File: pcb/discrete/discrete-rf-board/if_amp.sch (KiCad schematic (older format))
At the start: 46 parts, among them Q401 NSVT65011MW6T1G, Q402 Q_NPN_BCE, Q403 NSVT65011MW6T1G, U401 NLAS4157DFT2G, U402 NLAS4157DFT2G, U403 NLAS4157DFT2G, U404 NLAS4157DFT2G

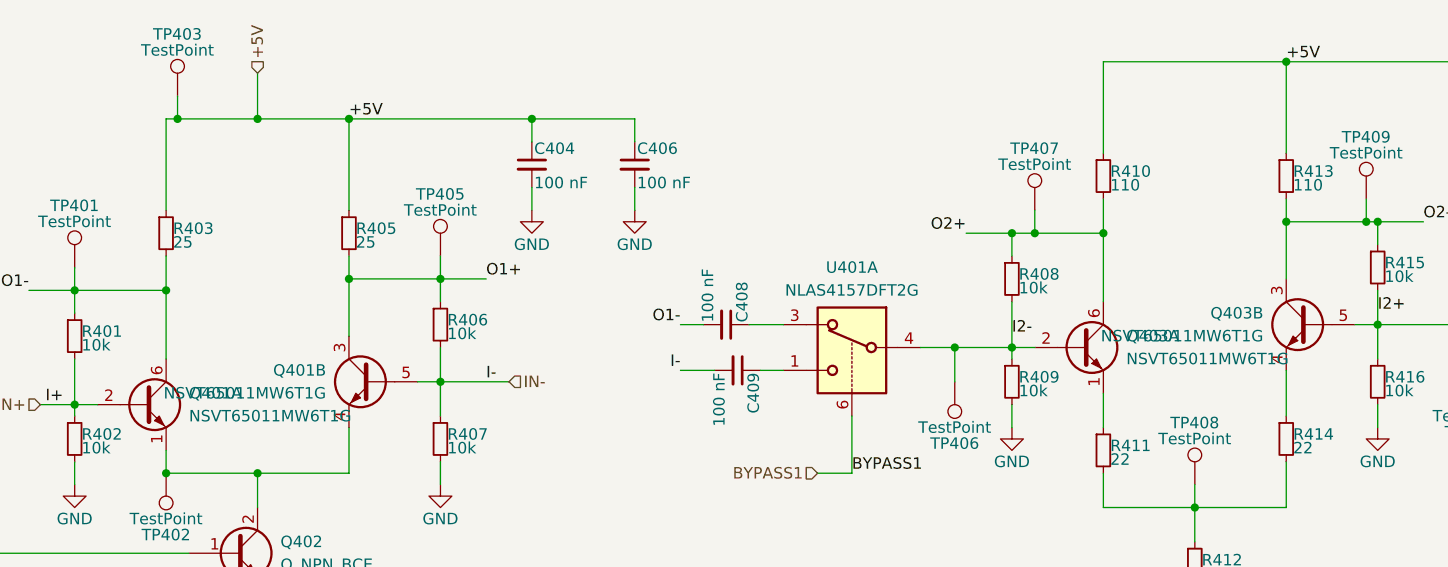
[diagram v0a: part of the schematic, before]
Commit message: Design DAC/ADC stages, pass out all control signals to top sheet
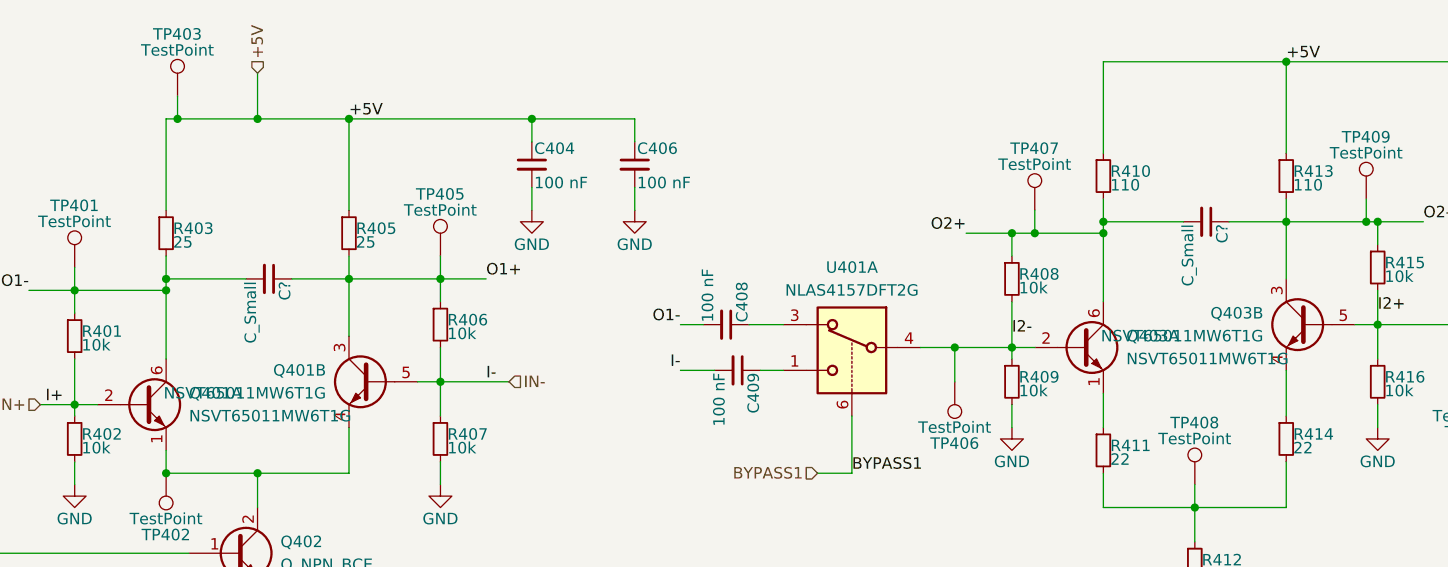
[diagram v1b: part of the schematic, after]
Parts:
- added C? (x2): C_Small, symbol Device:C_Small
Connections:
- net O1+: now also C?.1
- net O1-: now also C?.2
- net O2+: now also C?.2
- net O2-: now also C?.1
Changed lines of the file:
@@
 	1650 2500 2050 2500
 Wire Wire Line
-	2050 2500 2050 2350
+	2050 2500 2050 2450
 Wire Wire Line
 	2050 2800 2050 2500
@@
 	5750 2250 5850 2250
 Wire Wire Line
-	6150 2250 6150 2100
+	6150 2250 6150 2200
 Wire Wire Line
 	6150 2550 6150 2250
@@
 	2850 1750 3650 1750
 Connection ~ 2850 1750
+$Comp
+L Device:C_Small C?
+U 1 1 5DA03B3D
+P 2500 2450
+AR Path="/5CA6B0AA/5CC4DFC2/5DA03B3D" Ref="C?"  Part="1"
+AR Path="/5CA6B0AA/5CC9409A/5DA03B3D" Ref="C?"  Part="1"
+F 0 "C?" H 2510 2520 50  0000 L CNN
+F 1 "C_Small" H 2510 2370 50  0000 L CNN
+F 2 "" H 2500 2450 50  0001 C CNN
+F 3 "~" H 2500 2450 50  0001 C CNN
+	1    2500 2450
+	0    1    1    0
+$EndComp
+Wire Wire Line
+	2600 2450 2850 2450
+Wire Wire Line
+	2400 2450 2050 2450
+Connection ~ 2050 2450
+Wire Wire Line
+	2050 2450 2050 2350
+$Comp
+L Device:C_Small C?
+U 1 1 5DA0FE44
+P 6600 2200
+AR Path="/5CA6B0AA/5CC4DFC2/5DA0FE44" Ref="C?"  Part="1"
+AR Path="/5CA6B0AA/5CC9409A/5DA0FE44" Ref="C?"  Part="1"
+F 0 "C?" H 6610 2270 50  0000 L CNN
+F 1 "C_Small" H 6610 2120 50  0000 L CNN
+F 2 "" H 6600 2200 50  0001 C CNN
+F 3 "~" H 6600 2200 50  0001 C CNN
+	1    6600 2200
+	0    1    1    0
+$EndComp
+Wire Wire Line
+	6700 2200 6950 2200
+Wire Wire Line
+	6500 2200 6150 2200
+Connection ~ 6150 2200
+Wire Wire Line
+	6150 2200 6150 2100
 $EndSCHEMATC

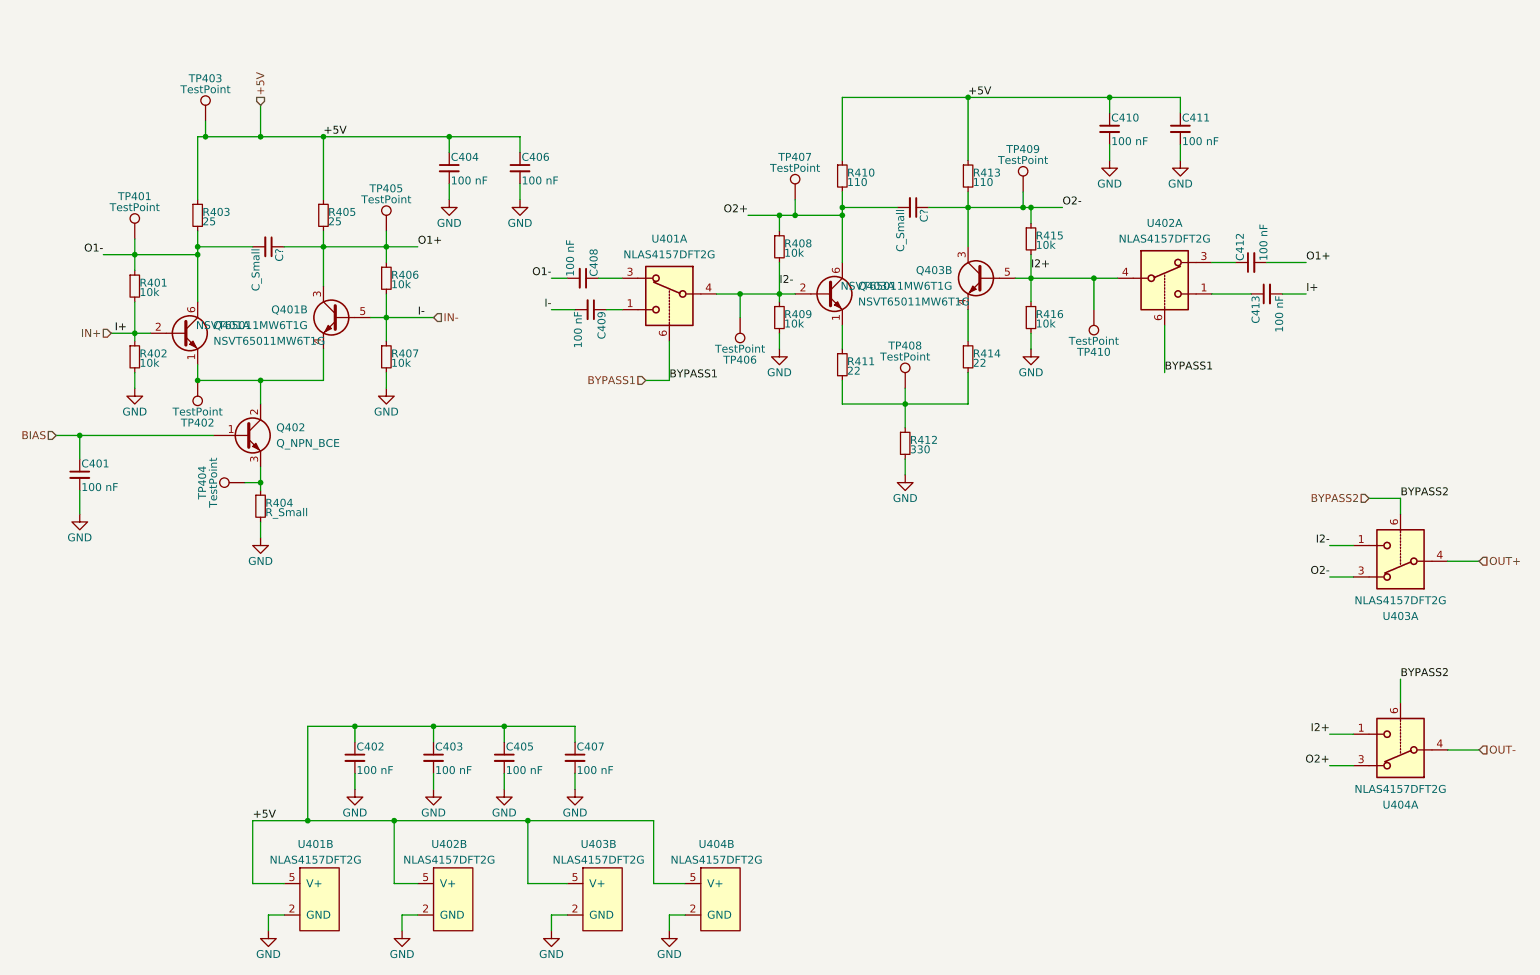
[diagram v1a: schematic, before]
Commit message: Wire out all control signals to connectors TODO PLL charge pump loop, bypass caps in attenuator circuit, antialiasing filter for ADC frontend
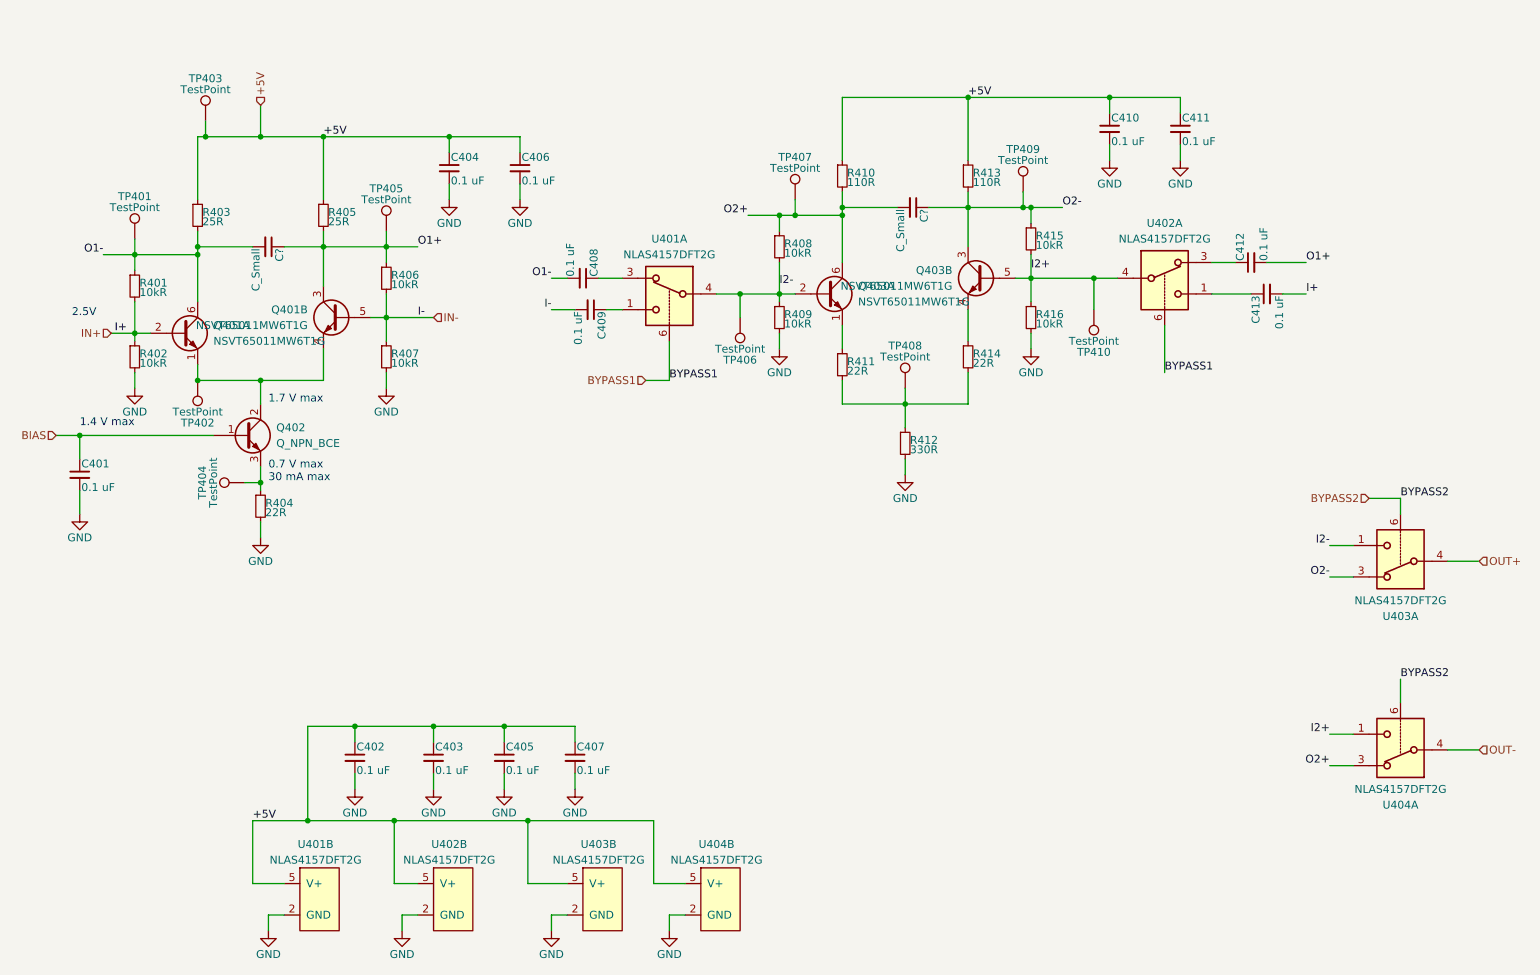
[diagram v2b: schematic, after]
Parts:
- C401, C402, C403, C404, C405, C406, C407, C408, C409, C410, C411, C412, C413: value 100 nF -> 0.1 uF
- R401, R402, R406, R407, R408, R409, R415, R416: value 10k -> 10kR
- R403, R405: value 25 -> 25R
- R404: value R_Small -> 22R
- R410, R413: value 110 -> 110R
- R411, R414: value 22 -> 22R
- R412: value 330 -> 330R
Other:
- note added: "0.7 V max\n30 mA max"
- note added: "1.4 V max"
- note added: "1.7 V max"
- note added: "2.5V"
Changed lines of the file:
@@
 $Descr A4 11693 8268
 encoding utf-8
-Sheet 4 19
+Sheet 10 19
 Title ""
 Date ""
@@
 AR Path="/5CA6B0AA/5CC9409A/5CC4F475" Ref="R603"  Part="1"
 F 0 "R403" H 2080 2270 50  0000 L CNN
-F 1 "25" H 2080 2210 50  0000 L CNN
+F 1 "25R" H 2080 2210 50  0000 L CNN
 F 2 "" H 2050 2250 50  0001 C CNN
 F 3 "~" H 2050 2250 50  0001 C CNN
@@
 AR Path="/5CA6B0AA/5CC9409A/5CC4F99A" Ref="R605"  Part="1"
 F 0 "R405" H 2880 2270 50  0000 L CNN
-F 1 "25" H 2880 2210 50  0000 L CNN
+F 1 "25R" H 2880 2210 50  0000 L CNN
 F 2 "" H 2850 2250 50  0001 C CNN
 F 3 "~" H 2850 2250 50  0001 C CNN
@@
 AR Path="/5CA6B0AA/5CC9409A/5CC50F59" Ref="R604"  Part="1"
 F 0 "R404" H 2480 4120 50  0000 L CNN
-F 1 "R_Small" H 2480 4060 50  0000 L CNN
+F 1 "22R" H 2480 4060 50  0000 L CNN
 F 2 "" H 2450 4100 50  0001 C CNN
 F 3 "~" H 2450 4100 50  0001 C CNN
@@
 AR Path="/5CA6B0AA/5CC9409A/5CC5132A" Ref="R601"  Part="1"
 F 0 "R401" H 1680 2720 50  0000 L CNN
-F 1 "10k" H 1680 2660 50  0000 L CNN
+F 1 "10kR" H 1680 2660 50  0000 L CNN
 F 2 "" H 1650 2700 50  0001 C CNN
 F 3 "~" H 1650 2700 50  0001 C CNN
@@
 AR Path="/5CA6B0AA/5CC9409A/5CC51AB5" Ref="R602"  Part="1"
 F 0 "R402" H 1680 3170 50  0000 L CNN
-F 1 "10k" H 1680 3110 50  0000 L CNN
+F 1 "10kR" H 1680 3110 50  0000 L CNN
 F 2 "" H 1650 3150 50  0001 C CNN
 F 3 "~" H 1650 3150 50  0001 C CNN
@@
 AR Path="/5CA6B0AA/5CC9409A/5CC51E44" Ref="R607"  Part="1"
 F 0 "R407" H 3280 3170 50  0000 L CNN
-F 1 "10k" H 3280 3110 50  0000 L CNN
+F 1 "10kR" H 3280 3110 50  0000 L CNN
 F 2 "" H 3250 3150 50  0001 C CNN
 F 3 "~" H 3250 3150 50  0001 C CNN
@@
 AR Path="/5CA6B0AA/5CC9409A/5CC52920" Ref="R606"  Part="1"
 F 0 "R406" H 3280 2670 50  0000 L CNN
-F 1 "10k" H 3280 2610 50  0000 L CNN
+F 1 "10kR" H 3280 2610 50  0000 L CNN
 F 2 "" H 3250 2650 50  0001 C CNN
 F 3 "~" H 3250 2650 50  0001 C CNN
@@
 AR Path="/5CA6B0AA/5CC9409A/5CC63FED" Ref="C601"  Part="1"
 F 0 "C401" H 1310 3970 50  0000 L CNN
-F 1 "100 nF" H 1310 3820 50  0000 L CNN
+F 1 "0.1 uF" H 1310 3820 50  0000 L CNN
 F 2 "" H 1300 3900 50  0001 C CNN
 F 3 "~" H 1300 3900 50  0001 C CNN
@@
 AR Path="/5CA6B0AA/5CC9409A/5CC7100E" Ref="R610"  Part="1"
 F 0 "R410" H 6180 2020 50  0000 L CNN
-F 1 "110" H 6180 1960 50  0000 L CNN
+F 1 "110R" H 6180 1960 50  0000 L CNN
 F 2 "" H 6150 2000 50  0001 C CNN
 F 3 "~" H 6150 2000 50  0001 C CNN
@@
 AR Path="/5CA6B0AA/5CC9409A/5CC71014" Ref="R613"  Part="1"
 F 0 "R413" H 6980 2020 50  0000 L CNN
-F 1 "110" H 6980 1960 50  0000 L CNN
+F 1 "110R" H 6980 1960 50  0000 L CNN
 F 2 "" H 6950 2000 50  0001 C CNN
 F 3 "~" H 6950 2000 50  0001 C CNN
@@
 AR Path="/5CA6B0AA/5CC9409A/5CC71026" Ref="R608"  Part="1"
 F 0 "R408" H 5780 2470 50  0000 L CNN
-F 1 "10k" H 5780 2410 50  0000 L CNN
+F 1 "10kR" H 5780 2410 50  0000 L CNN
 F 2 "" H 5750 2450 50  0001 C CNN
 F 3 "~" H 5750 2450 50  0001 C CNN
@@
 AR Path="/5CA6B0AA/5CC9409A/5CC7102C" Ref="R609"  Part="1"
 F 0 "R409" H 5780 2920 50  0000 L CNN
-F 1 "10k" H 5780 2860 50  0000 L CNN
+F 1 "10kR" H 5780 2860 50  0000 L CNN
 F 2 "" H 5750 2900 50  0001 C CNN
 F 3 "~" H 5750 2900 50  0001 C CNN
@@
 AR Path="/5CA6B0AA/5CC9409A/5CC71032" Ref="R616"  Part="1"
 F 0 "R416" H 7380 2920 50  0000 L CNN
-F 1 "10k" H 7380 2860 50  0000 L CNN
+F 1 "10kR" H 7380 2860 50  0000 L CNN
 F 2 "" H 7350 2900 50  0001 C CNN
 F 3 "~" H 7350 2900 50  0001 C CNN
@@
 AR Path="/5CA6B0AA/5CC9409A/5CC71038" Ref="R615"  Part="1"
 F 0 "R415" H 7380 2420 50  0000 L CNN
-F 1 "10k" H 7380 2360 50  0000 L CNN
+F 1 "10kR" H 7380 2360 50  0000 L CNN
 F 2 "" H 7350 2400 50  0001 C CNN
 F 3 "~" H 7350 2400 50  0001 C CNN
@@
 AR Path="/5CA6B0AA/5CC9409A/5CC78AA9" Ref="R612"  Part="1"
 F 0 "R412" H 6580 3720 50  0000 L CNN
-F 1 "330" H 6580 3660 50  0000 L CNN
+F 1 "330R" H 6580 3660 50  0000 L CNN
 F 2 "" H 6550 3700 50  0001 C CNN
 F 3 "~" H 6550 3700 50  0001 C CNN
@@
 AR Path="/5CA6B0AA/5CC9409A/5CC7FE22" Ref="R611"  Part="1"
 F 0 "R411" H 6180 3220 50  0000 L CNN
-F 1 "22" H 6180 3160 50  0000 L CNN
+F 1 "22R" H 6180 3160 50  0000 L CNN
 F 2 "" H 6150 3200 50  0001 C CNN
 F 3 "~" H 6150 3200 50  0001 C CNN
@@
 AR Path="/5CA6B0AA/5CC9409A/5CC80169" Ref="R614"  Part="1"
 F 0 "R414" H 6980 3170 50  0000 L CNN
-F 1 "22" H 6980 3110 50  0000 L CNN
+F 1 "22R" H 6980 3110 50  0000 L CNN
 F 2 "" H 6950 3150 50  0001 C CNN
 F 3 "~" H 6950 3150 50  0001 C CNN
@@
 AR Path="/5CA6B0AA/5CC9409A/5CC9409E" Ref="C608"  Part="1"
 F 0 "C408" H 4510 2720 50  0000 L CNN
-F 1 "100 nF" H 4510 2570 50  0000 L CNN
+F 1 "0.1 uF" H 4510 2570 50  0000 L CNN
 F 2 "" H 4500 2650 50  0001 C CNN
 F 3 "~" H 4500 2650 50  0001 C CNN
@@
 AR Path="/5CA6B0AA/5CC9409A/5CC959FD" Ref="C612"  Part="1"
 F 0 "C412" H 8760 2620 50  0000 L CNN
-F 1 "100 nF" H 8760 2470 50  0000 L CNN
+F 1 "0.1 uF" H 8760 2470 50  0000 L CNN
 F 2 "" H 8750 2550 50  0001 C CNN
 F 3 "~" H 8750 2550 50  0001 C CNN
@@
 AR Path="/5CA6B0AA/5CC9409A/5CC5931A" Ref="C609"  Part="1"
 F 0 "C409" H 4560 2920 50  0000 L CNN
-F 1 "100 nF" H 4560 2770 50  0000 L CNN
+F 1 "0.1 uF" H 4560 2770 50  0000 L CNN
 F 2 "" H 4550 2850 50  0001 C CNN
 F 3 "~" H 4550 2850 50  0001 C CNN
@@
 AR Path="/5CA6B0AA/5CC9409A/5CC646BF" Ref="C613"  Part="1"
 F 0 "C413" H 8860 2820 50  0000 L CNN
-F 1 "100 nF" H 8860 2670 50  0000 L CNN
+F 1 "0.1 uF" H 8860 2670 50  0000 L CNN
 F 2 "" H 8850 2750 50  0001 C CNN
 F 3 "~" H 8850 2750 50  0001 C CNN
@@
 AR Path="/5CA6B0AA/5CC9409A/5CC9DCE4" Ref="C602"  Part="1"
 F 0 "C402" H 3060 5770 50  0000 L CNN
-F 1 "100 nF" H 3060 5620 50  0000 L CNN
+F 1 "0.1 uF" H 3060 5620 50  0000 L CNN
 F 2 "" H 3050 5700 50  0001 C CNN
 F 3 "~" H 3050 5700 50  0001 C CNN
@@
 AR Path="/5CA6B0AA/5CC9409A/5CC9E1ED" Ref="C603"  Part="1"
 F 0 "C403" H 3560 5770 50  0000 L CNN
-F 1 "100 nF" H 3560 5620 50  0000 L CNN
+F 1 "0.1 uF" H 3560 5620 50  0000 L CNN
 F 2 "" H 3550 5700 50  0001 C CNN
 F 3 "~" H 3550 5700 50  0001 C CNN
@@
 AR Path="/5CA6B0AA/5CC9409A/5CC9E6BF" Ref="C605"  Part="1"
 F 0 "C405" H 4010 5770 50  0000 L CNN
-F 1 "100 nF" H 4010 5620 50  0000 L CNN
+F 1 "0.1 uF" H 4010 5620 50  0000 L CNN
 F 2 "" H 4000 5700 50  0001 C CNN
 F 3 "~" H 4000 5700 50  0001 C CNN
@@
 AR Path="/5CA6B0AA/5CC9409A/5CC9EAA6" Ref="C607"  Part="1"
 F 0 "C407" H 4460 5770 50  0000 L CNN
-F 1 "100 nF" H 4460 5620 50  0000 L CNN
+F 1 "0.1 uF" H 4460 5620 50  0000 L CNN
 F 2 "" H 4450 5700 50  0001 C CNN
 F 3 "~" H 4450 5700 50  0001 C CNN
@@
 AR Path="/5CA6B0AA/5CC9409A/5D57AB5D" Ref="C604"  Part="1"
 F 0 "C404" H 3660 2020 50  0000 L CNN
-F 1 "100 nF" H 3660 1870 50  0000 L CNN
+F 1 "0.1 uF" H 3660 1870 50  0000 L CNN
 F 2 "" H 3650 1950 50  0001 C CNN
 F 3 "~" H 3650 1950 50  0001 C CNN
@@
 AR Path="/5CA6B0AA/5CC9409A/5D57AB63" Ref="C606"  Part="1"
 F 0 "C406" H 4110 2020 50  0000 L CNN
-F 1 "100 nF" H 4110 1870 50  0000 L CNN
+F 1 "0.1 uF" H 4110 1870 50  0000 L CNN
 F 2 "" H 4100 1950 50  0001 C CNN
 F 3 "~" H 4100 1950 50  0001 C CNN
@@
 AR Path="/5CA6B0AA/5CC9409A/5D580ACE" Ref="C610"  Part="1"
 F 0 "C410" H 7860 1770 50  0000 L CNN
-F 1 "100 nF" H 7860 1620 50  0000 L CNN
+F 1 "0.1 uF" H 7860 1620 50  0000 L CNN
 F 2 "" H 7850 1700 50  0001 C CNN
 F 3 "~" H 7850 1700 50  0001 C CNN
@@
 AR Path="/5CA6B0AA/5CC9409A/5D580AD4" Ref="C611"  Part="1"
 F 0 "C411" H 8310 1770 50  0000 L CNN
-F 1 "100 nF" H 8310 1620 50  0000 L CNN
+F 1 "0.1 uF" H 8310 1620 50  0000 L CNN
 F 2 "" H 8300 1700 50  0001 C CNN
 F 3 "~" H 8300 1700 50  0001 C CNN
@@
 Wire Wire Line
 	6150 2200 6150 2100
+Text Notes 1250 2900 0    50   ~ 0
+2.5V
+Text Notes 2500 3450 0    50   ~ 0
+1.7 V max
+Text Notes 1300 3600 0    50   ~ 0
+1.4 V max
+Text Notes 2500 3950 0    50   ~ 0
+0.7 V max\n30 mA max
 $EndSCHEMATC

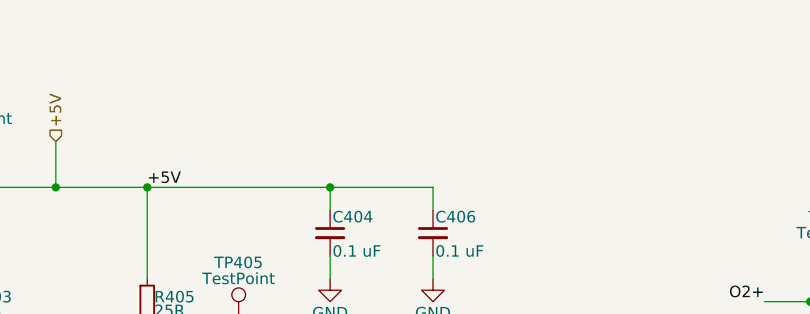
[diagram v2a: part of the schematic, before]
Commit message: Start work in footprinting everything
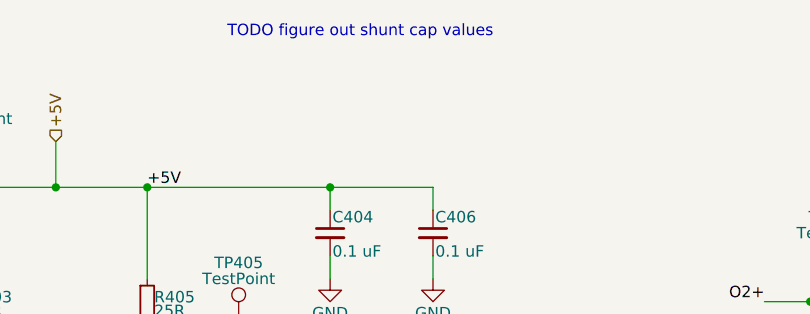
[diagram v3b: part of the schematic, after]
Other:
- note added: "TODO figure out shunt cap values"
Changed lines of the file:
@@
 Text Notes 2500 3950 0    50   ~ 0
 0.7 V max\n30 mA max
+Text Notes 3200 1100 0    50   ~ 0
+TODO figure out shunt cap values
 $EndSCHEMATC

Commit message: The footprintening continues
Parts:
- Q401: footprint (none) -> Package_TO_SOT_SMD:SOT-363_SC-70-6_Handsoldering; Mouser (none) -> 863-NSVT65011MW6T1G
- Q401, U401: footprint (none) -> Package_TO_SOT_SMD:SOT-363_SC-70-6_Handsoldering
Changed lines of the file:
@@
 F 0 "U401" H 2800 6950 50  0000 C CNN
 F 1 "NLAS4157DFT2G" H 2800 6850 50  0000 C CNN
-F 2 "" H 2800 6850 50  0001 C CNN
+F 2 "Package_TO_SOT_SMD:SOT-363_SC-70-6_Handsoldering" H 2800 6850 50  0001 C CNN
 F 3 "" H 2800 6850 50  0001 C CNN
 F 4 "863-NLAS4157DFT2G" H 2800 6600 50  0001 C CNN "Mouser"
@@
 F 0 "U401" H 5050 3100 50  0000 C CNN
 F 1 "NLAS4157DFT2G" H 5050 3000 50  0000 C CNN
-F 2 "" H 5050 3000 50  0001 C CNN
+F 2 "Package_TO_SOT_SMD:SOT-363_SC-70-6_Handsoldering" H 5050 3000 50  0001 C CNN
 F 3 "" H 5050 3000 50  0001 C CNN
 F 4 "863-NLAS4157DFT2G" H 5050 2750 50  0001 C CNN "Mouser"
@@
 F 0 "Q401" H 2150 3050 50  0000 L CNN
 F 1 "NSVT65011MW6T1G" H 2150 2950 50  0000 L CNN
-F 2 "" H 2150 3100 50  0001 C CNN
+F 2 "Package_TO_SOT_SMD:SOT-363_SC-70-6_Handsoldering" H 2150 3100 50  0001 C CNN
 F 3 "~" H 1950 3000 50  0001 C CNN
+F 4 " 863-NSVT65011MW6T1G" H 1950 3000 50  0001 C CNN "Mouser"
 	1    1950 3000
 	1    0    0    -1
@@
 F 0 "Q401" H 3150 2950 50  0000 L CNN
 F 1 "NSVT65011MW6T1G" H 3150 2850 50  0000 L CNN
-F 2 "" H 3150 3000 50  0001 C CNN
+F 2 "Package_TO_SOT_SMD:SOT-363_SC-70-6_Handsoldering" H 3150 3000 50  0001 C CNN
 F 3 "~" H 2950 2900 50  0001 C CNN
 	2    2950 2900
